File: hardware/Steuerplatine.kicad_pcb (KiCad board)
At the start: 2 copper layers, 110 x 110 mm, 62 parts, among them J1 Conn_01x02_Pin, J2 Conn_01x02_Pin, J3 Conn_01x06_Pin, Q1 BC848, Q2 BTA16-600B, Q3 BC848, U1 h0536, U2 LD1117S33TR_SOT223, U4 TL082

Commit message: done routing
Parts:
- removed J3: Conn_01x06_Pin, Connector_Phoenix_MC:PhoenixContact_MC_1,5_6-G-3.5_1x06_P3.50mm_Horizontal
- removed U1: h0536, Package_DIP:DIP-8_W7.62mm
- added R3: 10k, Resistor_SMD:R_0603_1608Metric, F.Cu at (421.0, 63.0)
- C2: value 4u7 -> 22u
- C3: value 470u -> 100n; footprint Capacitor_THT:CP_Radial_D8.0mm_P3.50mm -> Capacitor_SMD:C_0603_1608Metric
- L1: value 470u -> 1m
- R2: value 12k -> 4k
- R35: value 1k1 -> 2.49k
- U2: value LD1117S33TR_SOT223 -> LNK3202D; footprint Package_TO_SOT_SMD:SOT-223-3_TabPin2 -> Package_SO:PowerIntegrations_SO-8C
- U5: value ~ -> Seeed-ESP32C3; footprint RF_WiFi:MCU_Seeed_ESP32C3_solder -> RF_Module:MCU_Seeed_ESP32C3_HandSolder
- moved R1 53.5 mm to (450.0, 64.0)
- moved R44 49.2 mm to (439.0, 81.0), turned to 180 degrees
- moved R45 47.4 mm to (435.0, 81.0)
- moved R46 46.0 mm to (431.0, 81.0), turned to 180 degrees
- moved R47 45.0 mm to (427.0, 81.0)
- moved R48 44.4 mm to (423.0, 81.0), turned to 180 degrees
- moved R49 44.2 mm to (419.0, 81.0)
- moved R26 43.4 mm to (439.0, 84.0), turned to 180 degrees
- moved R27 41.7 mm to (435.0, 84.0)
- moved R28 40.4 mm to (431.0, 84.0), turned to 180 degrees
- moved R29 39.6 mm to (427.0, 84.0)
- moved R30 39.3 mm to (423.0, 84.0), turned to 180 degrees
- moved D1 38.5 mm to (434.0, 53.0), turned to 0 degrees
- moved R34 30.9 mm to (402.0, 139.0), turned to 0 degrees
- moved C1 28.2 mm to (424.0, 53.0)
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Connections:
- C14 pad 1: Net-(U1-IN) -> Net-(U2-D)
- C2 pad 1: Net-(U1-BP) -> Net-(D2-K)
- C3 pad 1: /+3V3 -> Net-(D3-K)
- C3 pad 2: /GND -> Net-(U2-BP/M)
- J1 pad 1: /L -> /+5V
- J1 pad 2: /+5V -> /L
- L1 pad 1: /+5V -> Net-(D3-K)
- L1 pad 2: Net-(D3-K) -> /+5V
- L2 pad 2: Net-(U1-IN) -> Net-(U2-D)
- R2 pad 1: Net-(D3-K) -> Net-(D2-K)
- R2 pad 2: Net-(U1-FB) -> Net-(U2-FB)
- R35 pad 1: Net-(D2-K) -> Net-(D3-K)
- R35 pad 2: Net-(U1-FB) -> Net-(U2-FB)
- RV1 pad 2: /AC_Filter/AC_L_FLT -> /L
- U2 pad 1: /GND -> Net-(U2-BP/M)
- U2 pad 2: /+3V3 -> Net-(U2-FB)
- U5 pad 19: unconnected-(U5-MTDO-Pad19) -> /+3V3
- U5 pad 20: /GND -> unconnected-(U5-MTMS-Pad20)
- U5 pad 22: unconnected-(U5-MTMS-Pad22) -> /GND
- U5 pad 23: /+3V3 -> unconnected-(U5-MTDO-Pad23)
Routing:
- net /+5V: track 0.00 -> 275.2 mm, vias 0 -> 2
- net /GND: track 0.00 -> 177.1 mm, vias 0 -> 2
- net Net-(Q2-G): track 0.00 -> 103.0 mm, vias 0 -> 1
- net Net-(Q2-A1): track 0.00 -> 76.2 mm, vias 0 -> 1
- net /Controller/SIG_CURRENT: track 0.00 -> 72.8 mm, vias 0 -> 4
- net /Controller/SIG_VOLTAGE: track 0.00 -> 63.9 mm, vias 0 -> 2
- net Net-(R49-Pad1): track 0.00 -> 63.3 mm
- net Net-(R30-Pad2): track 0.00 -> 57.0 mm
- net /+3V3: track 0.00 -> 39.6 mm, vias 0 -> 1
- net Net-(D3-K): track 0.00 -> 33.6 mm, vias 0 -> 1
- net /Controller/ZERO_CROSSING: track 0.00 -> 30.3 mm, vias 0 -> 2
- net /AC_Filter/AC_L_FLT: track 0.00 -> 28.4 mm
- net Net-(BZ1-+): track 0.00 -> 19.3 mm
- net Net-(D1-A): track 0.00 -> 17.5 mm
- net Net-(D1-K): track 0.00 -> 15.4 mm
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
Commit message: added pressure sensor
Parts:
- added U1: LPS28DFW, Sensor_Pressure:ST_LPS28DFW, F.Cu at (424.5, 130.0)
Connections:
- U5 pad 4: /Controller/pressure -> unconnected-(U5-D3-Pad4)
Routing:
- net /Controller/I2C_SDA: track 0.00 -> 13.2 mm
- net /Controller/I2C_SCL: track 0.00 -> 13.0 mm
- net /GND: track 177.1 -> 183.8 mm
- net /+3V3: track 39.6 -> 42.1 mm
- added copper zone on F.Cu, net Net-(D3-K)

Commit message: bugfix: triac output needs to confront L potential
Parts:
- F1: value 1.6A -> 7A
- R1: footprint Resistor_SMD:R_1206_3216Metric -> Resistor_SMD:R_2512_6332Metric
- moved R1 268.1 mm to (184.4, 100.8), turned to 135 degrees
- moved RV1 267.4 mm to (193.0, 128.8)
- moved C1 267.4 mm to (159.8, 94.0)
- moved C14 267.4 mm to (146.8, 93.8)
- moved C2 267.4 mm to (157.8, 107.0)
- moved C3 267.4 mm to (153.8, 106.0)
- moved C4 267.4 mm to (156.8, 114.4)
- moved D1 267.4 mm to (169.8, 94.0)
- moved D11 267.4 mm to (154.8, 168.0)
- moved D2 267.4 mm to (163.8, 103.0)
- moved D3 267.4 mm to (149.8, 115.0)
- moved F1 267.4 mm to (190.8, 111.0)
- moved H2 267.4 mm to (176.0, 180.3)
- moved H3 267.4 mm to (131.0, 102.0)
- moved H4 267.4 mm to (176.6, 102.0)
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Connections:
- C13 pad 1: /AC_Filter/AC_L_FLT -> /L_filt
- F1 pad 2: /AC_Filter/AC_L_FLT -> /L_filt
- J2 pad 1: /+5V -> /L_filt
- R1 pad 1: /AC_Filter/AC_L_FLT -> /L_filt
- R26 pad 1: /AC_Filter/AC_L_FLT -> /L_filt
- R44 pad 1: /AC_Filter/AC_L_FLT -> /L_filt
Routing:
- net Net-(Q2-G): track 103.0 -> 0.00 mm, vias 1 -> 0
- net /+5V: track 275.2 -> 180.6 mm
- net /L_filt: track 0.00 -> 90.0 mm
- net /Controller/SIG_CURRENT: track 72.8 -> 0.00 mm, vias 4 -> 0
- net Net-(Q2-A1): track 76.2 -> 6.74 mm, vias 1 -> 0
- net /GND: track 183.8 -> 115.7 mm
- net /Controller/SIG_VOLTAGE: track 63.9 -> 0.00 mm, vias 2 -> 0
- net /+3V3: track 42.1 -> 0.00 mm, vias 1 -> 0
- net /Controller/ZERO_CROSSING: track 30.3 -> 0.00 mm, vias 2 -> 0
- net /AC_Filter/AC_L_FLT: track 28.4 -> 0.00 mm
- net Net-(BZ1-+): track 19.3 -> 0.00 mm
- net /L: track 14.9 -> 32.8 mm, vias 0 -> 1
- net /Controller/I2C_SDA: track 13.2 -> 0.00 mm
- net /Controller/I2C_SCL: track 13.0 -> 0.00 mm
- net Net-(U4B-+): track 13.0 -> 0.00 mm
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
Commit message: added some zones
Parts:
- F1: footprint Fuse:Fuse_Schurter_UMZ250 -> Fuse:Fuse_2512_6332Metric
- moved R26 38.2 mm to (165.2, 160.5)
- moved R27 38.2 mm to (161.2, 160.5)
- moved R28 38.2 mm to (157.2, 160.5)
- moved R29 38.2 mm to (153.2, 160.5)
- moved R30 38.2 mm to (149.2, 160.5)
- moved R44 38.2 mm to (165.2, 157.5)
- moved R45 38.2 mm to (161.2, 157.5)
- moved R46 38.2 mm to (157.2, 157.5)
- moved R47 38.2 mm to (153.2, 157.5)
- moved R48 38.2 mm to (149.2, 157.5)
- moved R49 38.2 mm to (145.2, 157.5)
- moved R36 34.1 mm to (190.8, 169.5), turned to 0 degrees
- moved F1 27.9 mm to (187.2, 138.8), turned to -90 degrees
- moved L1 22.5 mm to (143.5, 105.5), turned to 180 degrees
- moved D1 18.7 mm to (187.0, 101.2), turned to -45 degrees
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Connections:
- C13 pad 1: /L_filt -> /L
- J1 pad 1: /+5V -> /L
- J1 pad 2: /L -> /+5V
- J2 pad 1: /L_filt -> /Triac/TRIAC_OUTPUT
- J2 pad 2: /Triac/TRIAC_OUTPUT -> /L_filt
- U1 pad 4: unconnected-(U1-INT_DRDY-Pad4) -> /Controller/pressure_interrupt
- U1 pad 7: unconnected-(U1-PAD2LID-Pad7) -> /GND
- U5 pad 7: unconnected-(U5-D6-Pad7) -> /Controller/pressure_interrupt
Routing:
- net Net-(R30-Pad2): track 61.7 -> 0.00 mm
- net Net-(R49-Pad1): track 55.4 -> 0.00 mm
- net /L_filt: track 90.0 -> 49.9 mm, vias 0 -> 14
- net /L: track 32.8 -> 0.00 mm, vias 1 -> 14
- net Net-(D3-K): track 33.6 -> 9.15 mm
- net /+5V: track 180.6 -> 195.3 mm
- net Net-(D1-K): track 15.4 -> 28.0 mm
- net /GND: track 115.7 -> 127.0 mm
- net /Triac/TRIAC_OUTPUT: track 15.3 -> 5.36 mm
- net Net-(U2-D): track 10.2 -> 18.7 mm
- net Net-(D1-A): track 12.0 -> 4.79 mm
- net Net-(Q2-A1): track 6.74 -> 0.00 mm
- net Net-(R48-Pad2): track 2.35 -> 0.00 mm
- net Net-(R47-Pad1): track 2.35 -> 0.00 mm
- net Net-(R46-Pad2): track 2.35 -> 0.00 mm
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- added copper zone on B.Cu, net /+5V
- added copper zone on F.Cu, net /+5V
- added copper zone on B.Cu, net /L
- added copper zone on F.Cu, net /L
- added copper zone on B.Cu, net /L_filt
- added copper zone on F.Cu, net /L_filt
- added copper zone on B.Cu, net Net-(Q2-A1)
- added copper zone on F.Cu, net Net-(Q2-A1)

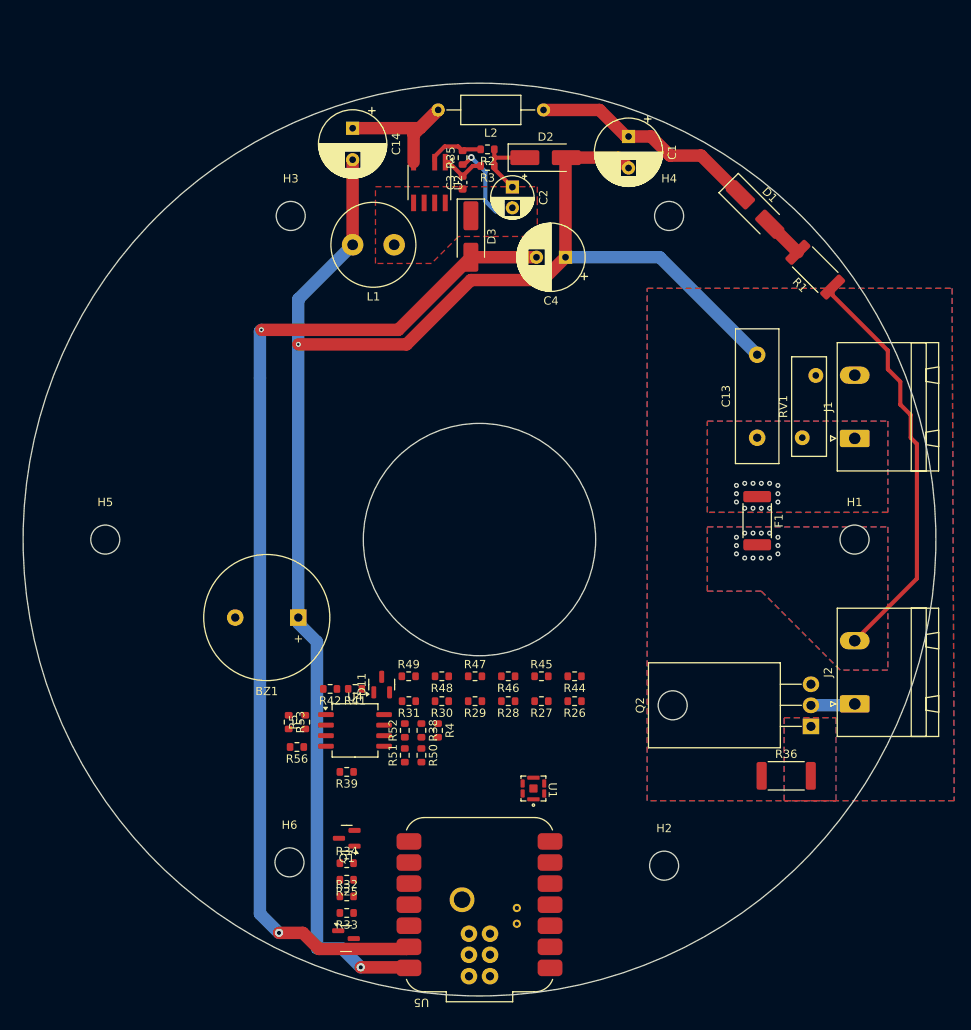
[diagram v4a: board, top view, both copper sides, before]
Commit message: added some datasheets
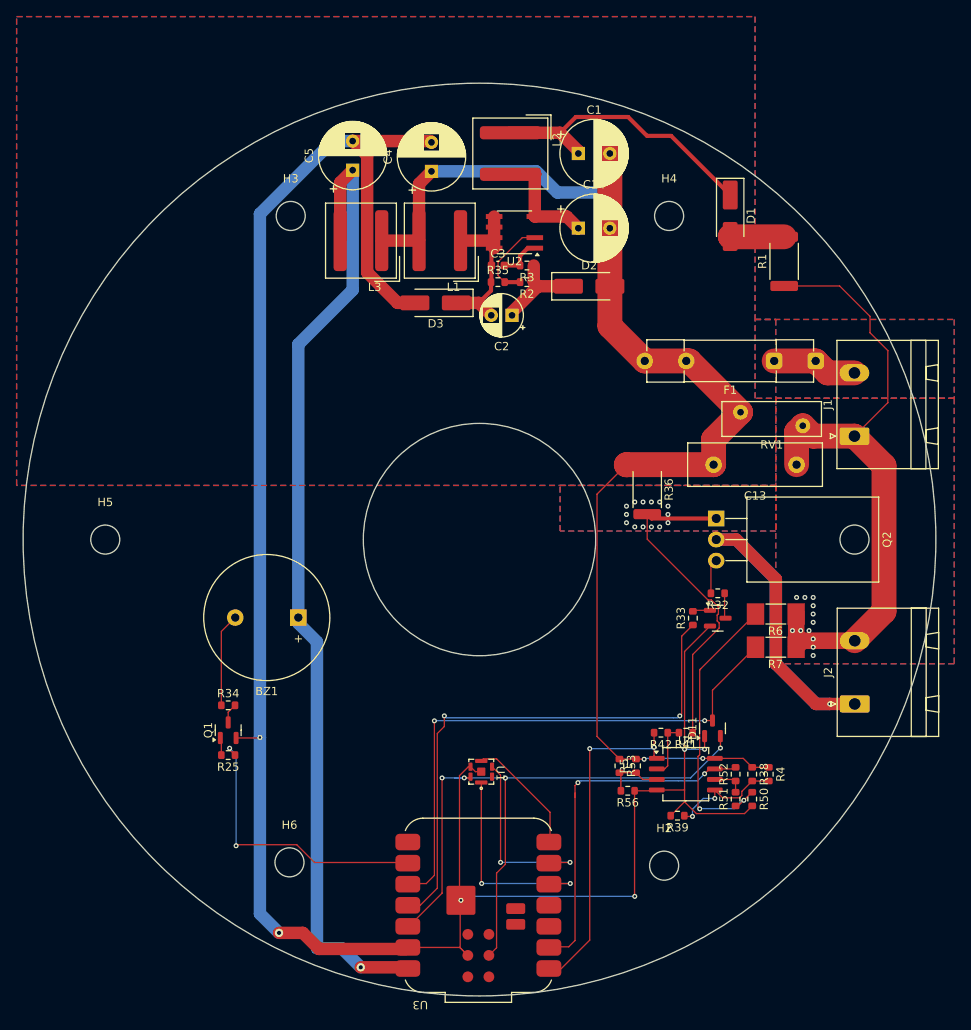
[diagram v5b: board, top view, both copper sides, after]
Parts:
- removed H1: MountingHole, MountingHole:MountingHole_3.5mm
- removed R26, R27, R28, R29, R30, R31, R44, R45, R46, R47, R48, R49: 47k, Resistor_SMD:R_0603_1608Metric
- removed U5: Seeed-ESP32C3, RF_Module:MCU_Seeed_ESP32C3_HandSolder
- added C5: 220u, Capacitor_THT:CP_Radial_D8.0mm_P3.50mm, F.Cu at (138.5, 96.5)
- added L3: 1m, Inductor_SMD:L_Wuerth_WE-XHMI-8080, F.Cu at (139.5, 105.0)
- added R6: 270k, Resistor_SMD:R_MELF_MMB-0207, F.Cu at (189.5, 150.0)
- added R7: 270k, Resistor_SMD:R_MELF_MMB-0207, F.Cu at (189.5, 154.0)
- added U3: Seeed-ESP32C3, RF_Module:MCU_Seeed_ESP32C3, F.Cu at (153.7, 185.1)
- F1: value 7A -> 10A; footprint Fuse:Fuse_2512_6332Metric -> Fuse:Fuseholder_Clip-5x20mm_Schurter_CQM_Inline_P20.60x5.00mm_D1.00mm_Horizontal
- L1: footprint Inductor_THT:L_Radial_D10.0mm_P5.00mm_Fastron_07P -> Inductor_SMD:L_Wuerth_WE-XHMI-8080
- L2: value 2.2mH -> 1m; footprint Inductor_THT:L_Axial_L7.0mm_D3.3mm_P12.70mm_Horizontal_Fastron_MICC -> Inductor_SMD:L_Wuerth_WE-XHMI-8080
- moved Q3 59.1 mm to (182.5, 150.5)
- moved R32 57.7 mm to (182.5, 147.5), turned to 180 degrees
- moved R33 54.8 mm to (179.5, 150.5), turned to 90 degrees
- moved D11 40.2 mm to (181.9, 163.8)
- moved R38 40.2 mm to (186.7, 169.3)
- moved R39 40.2 mm to (177.7, 174.3)
- moved R4 40.2 mm to (188.7, 169.3)
- moved R41 40.2 mm to (178.7, 164.3)
- moved R42 40.2 mm to (175.7, 164.3)
- moved R5 40.2 mm to (172.7, 168.3)
- moved R50 40.2 mm to (186.7, 172.3)
- moved R51 40.2 mm to (184.7, 172.3)
- moved R52 40.2 mm to (184.7, 169.3)
- moved R53 40.2 mm to (170.7, 168.3)
- moved R56 40.2 mm to (171.7, 171.3)
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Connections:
- C1 pad 2: /+5V -> /N_filt
- C13 pad 2: /+5V -> /N_filt
- C14 pad 2: /+5V -> /N_filt
- C4 pad 1: /+5V -> /N_filt
- D2 pad 2: /+5V -> /N_filt
- F1 pad 1: /L -> /N
- F1 pad 2: /L_filt -> /N_filt
- J1 pad 2: /+5V -> /N
- J2 pad 2: /L_filt -> /L
- L1 pad 2: /+5V -> /N_filt
- R1 pad 1: /L_filt -> /L
- R36 pad 1: /+5V -> /N_filt
- R38 pad 1: /+5V -> /N_filt
- R4 pad 1: /+5V -> /N_filt
- R5 pad 2: /+5V -> /N_filt
- R53 pad 1: /+5V -> /N_filt
- RV1 pad 1: /+5V -> /N_filt
- U4 pad 8: /+5V -> /N_filt
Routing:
- net /N_filt: track 0.00 -> 162.9 mm, vias 0 -> 2
- net /GND: track 127.0 -> 266.3 mm, vias 2 -> 6
- net /+3V3: track 0.00 -> 80.2 mm, vias 0 -> 4
- net /L: track 0.00 -> 79.6 mm, vias 14 -> 12
- net /+5V: track 195.3 -> 118.6 mm, vias 2 -> 1
- net /Controller/ZERO_CROSSING: track 0.00 -> 66.6 mm, vias 0 -> 2
- net /Controller/TRIAC_GATE: track 0.00 -> 65.7 mm, vias 0 -> 2
- net /Triac/TRIAC_OUTPUT: track 5.36 -> 59.0 mm, vias 0 -> 1
- net /L_filt: track 49.9 -> 0.00 mm, vias 14 -> 0
- net /Controller/SIG_VOLTAGE: track 0.00 -> 42.7 mm, vias 0 -> 2
- net /Controller/SIG_CURRENT: track 0.00 -> 40.5 mm, vias 0 -> 2
- net Net-(Q2-A1): track 0.00 -> 40.1 mm, vias 0 -> 14
- net Net-(R50-Pad1): track 0.00 -> 35.0 mm, vias 0 -> 2
- net /Controller/SUMMER: track 0.00 -> 34.9 mm, vias 0 -> 2
- net /Controller/I2C_SDA: track 0.00 -> 25.3 mm, vias 0 -> 2
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- added copper zone on B.Cu, net /N
- added copper zone on F.Cu, net /N
- removed copper zone on B.Cu, net /L_filt
- removed copper zone on F.Cu, net /L_filt
- removed copper zone on F.Cu, net Net-(D3-K)

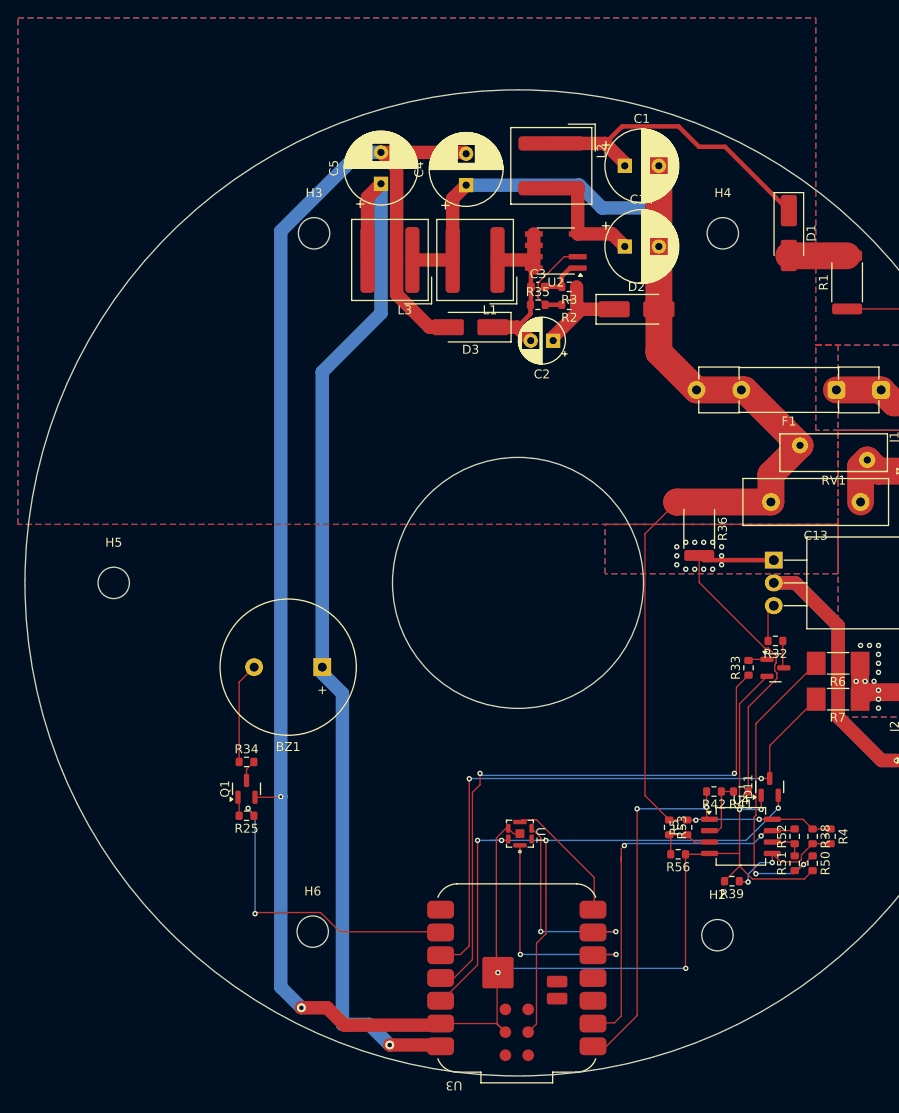
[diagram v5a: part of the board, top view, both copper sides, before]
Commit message: some more rules and routings
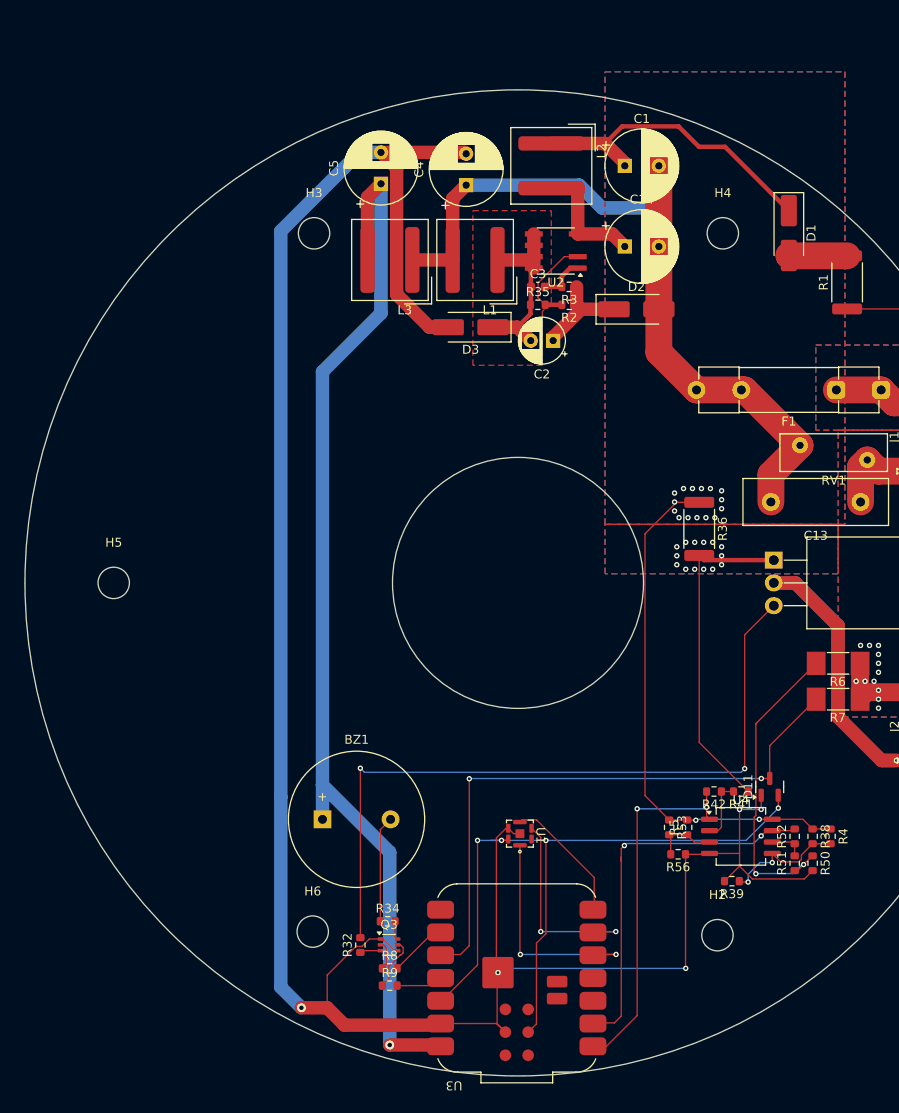
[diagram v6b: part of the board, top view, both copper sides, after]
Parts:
- removed Q1: BC848, Package_TO_SOT_SMD:SOT-23
- removed R25, R33: 4k7, Resistor_SMD:R_0603_1608Metric
- added R8: 470, Resistor_SMD:R_0603_1608Metric, F.Cu at (139.5, 184.0)
- added R9: 470, Resistor_SMD:R_0603_1608Metric, F.Cu at (139.5, 185.9)
- Q3: value BC848 -> BC847BS; footprint Package_TO_SOT_SMD:SOT-23 -> Package_TO_SOT_SMD:SOT-363_SC-70-6
- moved R32 57.4 mm to (136.2, 181.4), turned to 90 degrees
- moved Q3 53.0 mm to (139.4, 181.4)
- moved R34 23.7 mm to (139.2, 178.8)
- moved BZ1 17.0 mm to (132.0, 167.4), turned to 0 degrees
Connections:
- Q3 pad 1: Net-(Q3-B) -> /GND
- Q3 pad 2: /GND -> Net-(Q3A-B1)
- Q3 pad 3: Net-(Q3-C) -> /Controller/TRIAC_GATE
- R32 pad 1: Net-(Q3-C) -> /Controller/TRIAC_GATE
- R34 pad 2: Net-(Q1-C) -> Net-(Q3A-C1)
- U3 pad 11: /Controller/TRIAC_GATE -> /Controller/triac
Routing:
- net Net-(Q2-G): track 4.20 -> 81.7 mm, vias 0 -> 2
- net /Controller/TRIAC_GATE: track 65.7 -> 2.33 mm, vias 2 -> 0
- net /Controller/SUMMER: track 34.9 -> 6.51 mm, vias 2 -> 0
- net /N_filt: track 162.9 -> 155.2 mm, vias 2 -> 17
- net Net-(Q3B-B2): track 0.00 -> 6.02 mm
- net /GND: track 266.3 -> 261.0 mm, vias 6 -> 5
- net /Controller/triac: track 0.00 -> 5.20 mm
- net Net-(Q3A-B1): track 0.00 -> 3.29 mm
- net Net-(Q3-C): track 3.05 -> 0.00 mm
- net Net-(Q2-A1): track 40.1 -> 37.1 mm
- net Net-(Q1-C): track 2.40 -> 0.00 mm
- net Net-(Q3-B): track 2.11 -> 0.00 mm
- net Net-(Q1-B): track 2.11 -> 0.00 mm
- net Net-(Q3A-C1): track 0.00 -> 2.09 mm
- net /+5V: track 118.6 -> 120.7 mm
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- added copper zone on B.Cu, net /N_filt
- added copper zone on F.Cu, net /N_filt
- added copper zone on F.Cu, net Net-(D3-K)
- removed copper zone on B.Cu, net /+5V
- removed copper zone on F.Cu, net /+5V
